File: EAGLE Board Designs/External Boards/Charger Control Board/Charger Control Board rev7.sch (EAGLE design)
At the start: 109 parts, among them K1 RELAY_DPDT, K2 RELAY_DPDT, K3 RELAY_DPDT, K4 RELAY_SOLIDSTATE_NO_, U1 VOLTAGE_REGULATOR_SOT-223_5V, U2 MCP2562FD, U3 LOGICGATE_BUFFER, U4 MCP2562FD, U7 ADM823

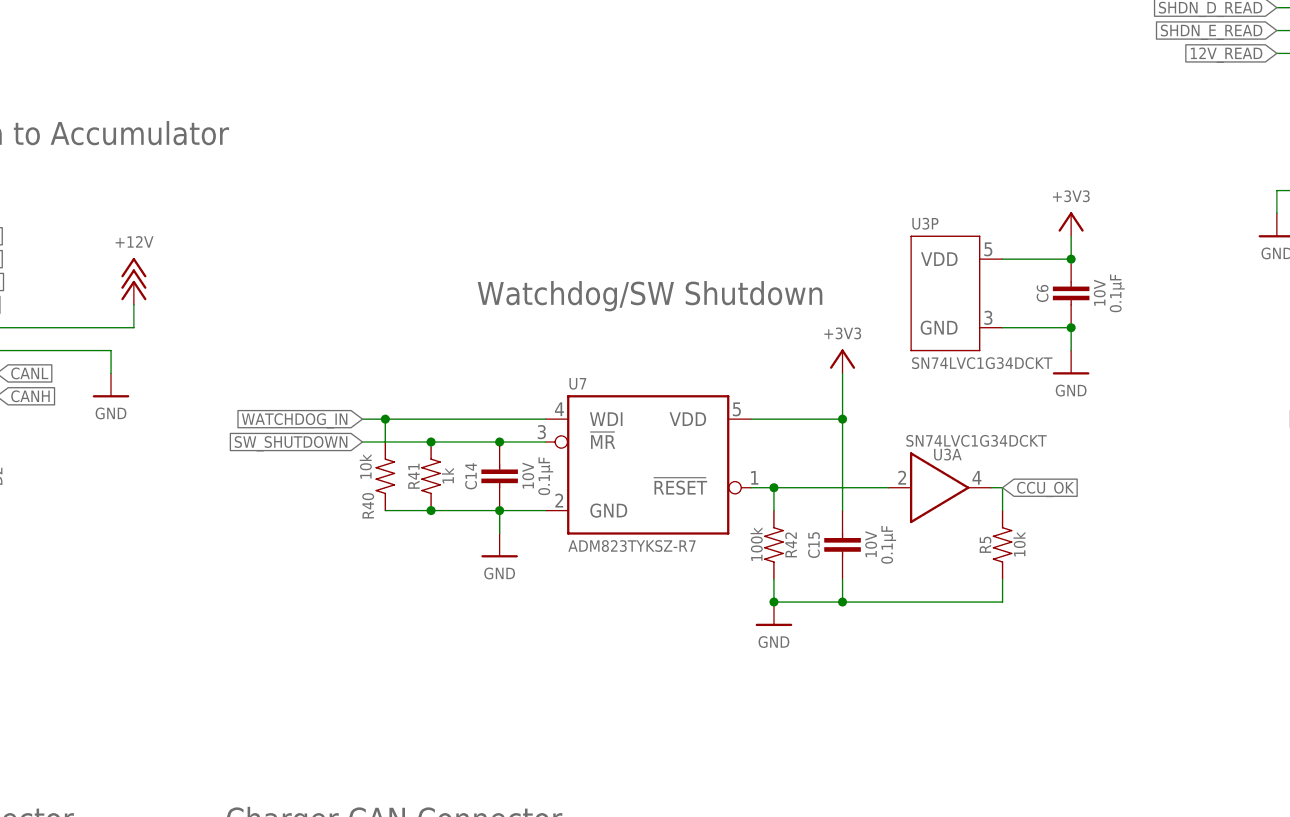
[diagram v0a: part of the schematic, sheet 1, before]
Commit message: Cleaned up schematic
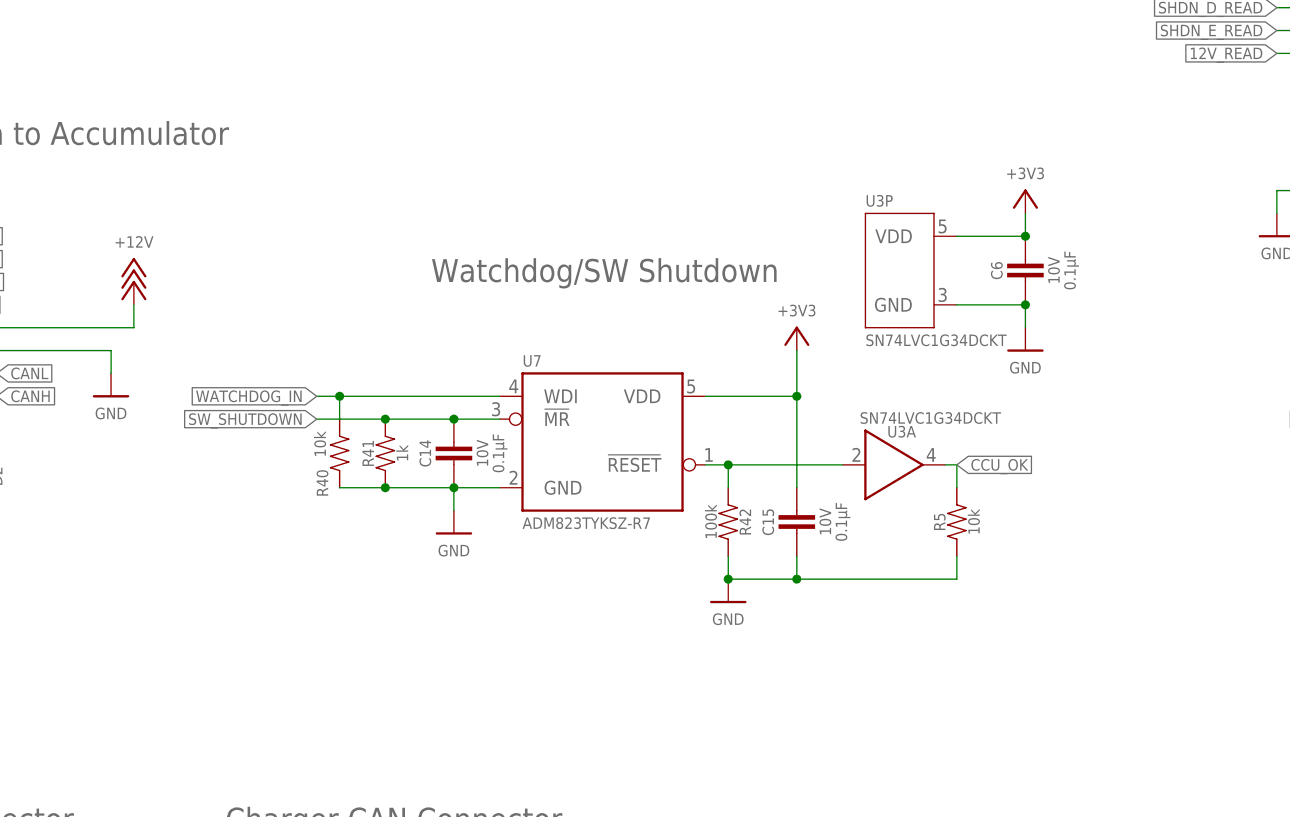
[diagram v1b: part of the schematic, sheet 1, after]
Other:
- moved on the sheet: C14, C15, C6, R40, R41, R42, R5, U3A, U3P, U7

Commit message: Fixed conflicting net
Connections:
- removed net N$7: C3.1, C5.1
- net GND: now also C3.1, C5.1
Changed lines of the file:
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@@
 <part name="P12" library="HyTechSupplies" deviceset="+3V3" device=""/>
 <part name="P13" library="HyTechSupplies" deviceset="+5V" device=""/>
-<part name="P15" library="HyTechSupplies" deviceset="GND" device=""/>
 <part name="P16" library="HyTechSupplies" deviceset="+3V3" device=""/>
 <part name="C3" library="HyTechDevices" deviceset="CAPACITOR_?_*" device="0603" technology="10V_0.1UF"/>
@@
 <part name="C6" library="HyTechDevices" deviceset="CAPACITOR_?_*" device="0603" technology="10V_0.1UF"/>
 <part name="R1" library="HyTechDevices" deviceset="RESISTOR_?_*" device="0603" technology="240"/>
+<part name="P15" library="HyTechSupplies" deviceset="GND" device=""/>
 </parts>
 <sheets>
@@
 <attribute name="VALUE" x="147.32" y="175.26" size="1.27" layer="96" align="bottom-center"/>
 </instance>
-<instance part="P15" gate="1" x="165.1" y="149.86" smashed="yes">
-<attribute name="VALUE" x="165.1" y="148.59" size="1.27" layer="96" align="top-center"/>
-</instance>
 <instance part="P16" gate="G$1" x="119.38" y="193.04" smashed="yes">
 <attribute name="VALUE" x="119.38" y="194.31" size="1.27" layer="96" align="bottom-center"/>
@@
 <attribute name="VOLTAGE" x="154.94" y="100.33" size="1.27" layer="96" rot="MR270" align="top-center"/>
 <attribute name="CAPACITANCE" x="156.718" y="100.33" size="1.27" layer="96" rot="MR270" align="top-center"/>
+</instance>
+<instance part="P15" gate="1" x="165.1" y="149.86" smashed="yes">
+<attribute name="VALUE" x="165.1" y="148.59" size="1.27" layer="96" align="top-center"/>
 </instance>
 </instances>
@@
 <junction x="152.4" y="96.52"/>
 </segment>
+<segment>
+<wire x1="157.48" y1="152.4" x2="165.1" y2="152.4" width="0.1524" layer="91"/>
+<pinref part="C3" gate="G$1" pin="1"/>
+<wire x1="165.1" y1="154.94" x2="165.1" y2="152.4" width="0.1524" layer="91"/>
+<pinref part="C5" gate="G$1" pin="1"/>
+<pinref part="P15" gate="1" pin="GND"/>
+<junction x="165.1" y="152.4"/>
+</segment>
 </net>
 <net name="N$1" class="0">
@@
 </segment>
 </net>
-<net name="N$7" class="0">
-<segment>
-<wire x1="157.48" y1="152.4" x2="165.1" y2="152.4" width="0.1524" layer="91"/>
-<pinref part="P15" gate="1" pin="GND"/>
-<pinref part="C3" gate="G$1" pin="1"/>
-<wire x1="165.1" y1="154.94" x2="165.1" y2="152.4" width="0.1524" layer="91"/>
-<junction x="165.1" y="152.4"/>
-<pinref part="C5" gate="G$1" pin="1"/>
-</segment>
-</net>

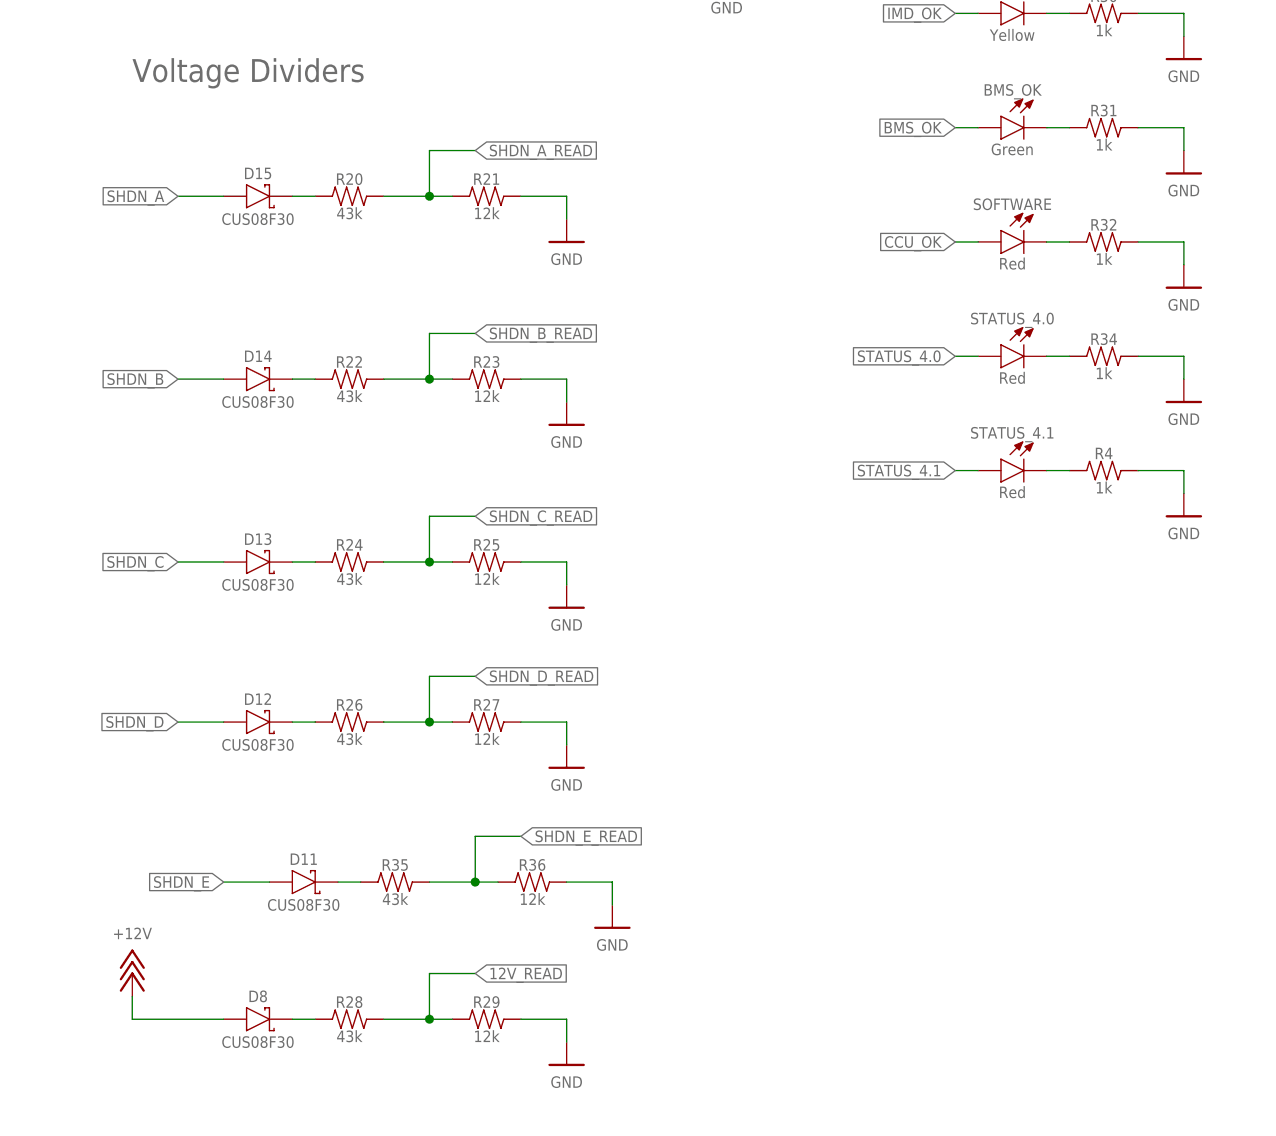
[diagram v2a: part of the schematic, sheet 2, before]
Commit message: Added charger interlock to shutdown circuit, removed diodes from voltage dividers
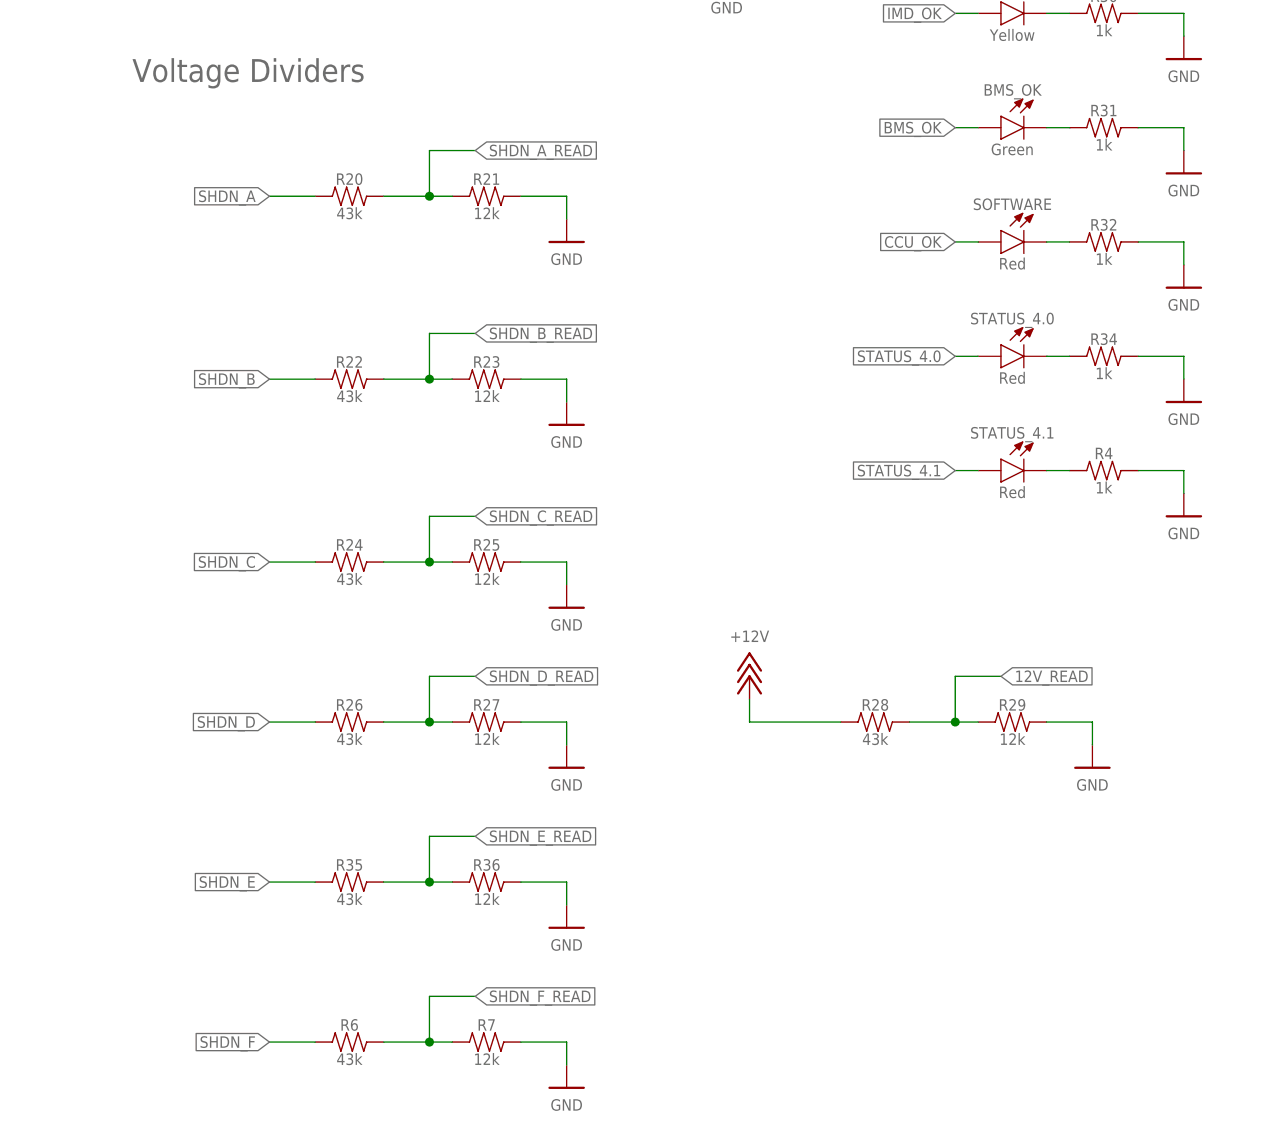
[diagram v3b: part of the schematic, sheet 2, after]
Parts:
- removed D11, D12, D13, D14, D15, D8: SCHOTTKY_SOD323_30V, HyTechDevices:SCHOTTKY_SOD323_30V
- added R6: RESISTOR_0603_43K, HyTechDevices:RESISTOR_0603_43K
- added R7: RESISTOR_0603_12K, HyTechDevices:RESISTOR_0603_12K
- CHG_CAN: value CONNECTOR-CAN_NF_T_V_BLACK -> CONNECTOR-6_NF_T_V_BLACK; device HyTechDevices:CONNECTOR-CAN_NF_T_V_BLACK -> HyTechDevices:CONNECTOR-6_NF_T_V_BLACK
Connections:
- removed net N$24: D14.C, R22.1
- removed net N$25: D15.C, R20.1
- removed net N$26: D13.C, R24.1
- removed net N$27: D12.C, R26.1
- removed net N$28: D8.C, R28.1
- removed net N$34: D11.C, R35.1
- new net SHDN_F: CHG_CAN.2, MAIN_CONNECTOR.7, MAIN_CONNECTOR.8, R6.1
- new net SHDN_F_READ: A1.A5, A2.A5, R6.2, R7.1
- net +12V: now also R28.1; no longer D8.A
- net 12V_READ: now also A1.A6, A2.A6; no longer A1.A5, A2.A5
- net CANH: now also CHG_CAN.4; no longer CHG_CAN.CANH
- net CANL: now also CHG_CAN.5; no longer CHG_CAN.CANL
- net GND: now also CHG_CAN.6, R7.2; no longer CHG_CAN.GND
- net SHDN_A: now also R20.1; no longer D15.A
- net SHDN_B: now also R22.1; no longer D14.A
- net SHDN_C: now also R24.1; no longer D13.A
- net SHDN_D: now also R26.1; no longer D12.A
- net SHDN_E: now also CHG_CAN.3, R35.1; no longer D11.A, MAIN_CONNECTOR.7, MAIN_CONNECTOR.8
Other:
- moved on the sheet: R28, R29, R35, R36

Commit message: Initial board design rev7
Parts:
- added R33: RESISTOR_0603_1K, HyTechDevices:RESISTOR_0603_1K
- added SHUTDOWN_F: LED_0603_RED, HyTechDevices:LED_0603_RED
- 4.1_ONLY, CAN_TERM: value JUMPER_NANOFIT_SMD_VERTICAL_BLACK -> JUMPER__; device HyTechDevices:JUMPER_NANOFIT_SMD_VERTICAL_BLACK -> HyTechDevices:JUMPER__
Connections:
- new net N$3: R33.1, SHUTDOWN_F.C
- net +12V: no longer TP2.P$1
- net +3V3: no longer TP11.P$1
- net +5V: no longer TP1.P$1
- net BMS_OK: no longer TP10.P$1
- net CCU_OK: no longer TP8.P$1
- net GND: now also R33.2; no longer TP12.P$1
- net IMD_OK: no longer TP9.P$1
- net SHDN_A: no longer TP3.P$1
- net SHDN_B: no longer TP4.P$1
- net SHDN_C: no longer TP5.P$1
- net SHDN_D: no longer TP6.P$1
- net SHDN_E: now also MAIN_CONNECTOR.7; no longer TP7.P$1
- net SHDN_F: now also SHUTDOWN_F.A; no longer MAIN_CONNECTOR.7
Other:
- moved on the sheet: R28, R29, TP1, TP10, TP11, TP12, TP2, TP3, TP4, TP5, TP6, TP7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
